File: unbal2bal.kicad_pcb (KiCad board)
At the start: 2 copper layers, 76 x 90 mm, 36 parts, among them J1 RCJ-041, J2 NRJ3HF-1, J3 Mini-DIN-3, J4 Mini-DIN-4, U1 LM4562

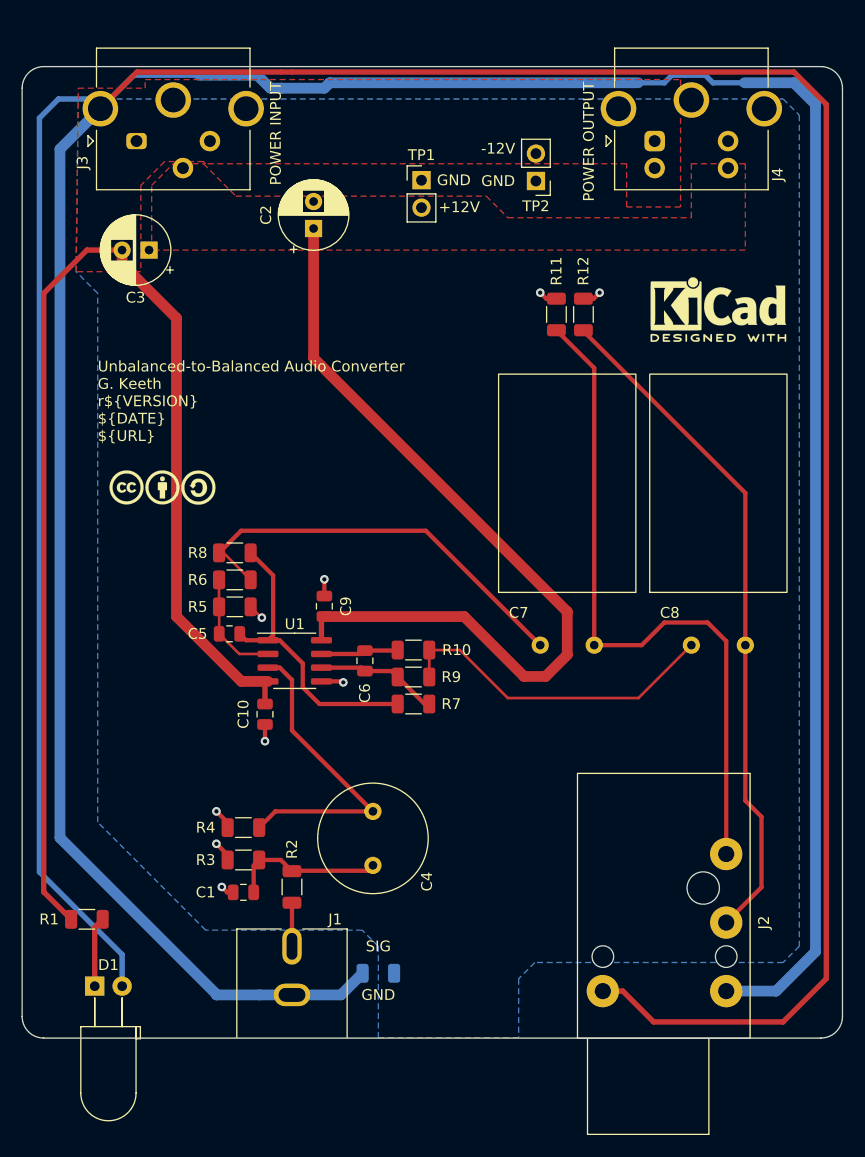
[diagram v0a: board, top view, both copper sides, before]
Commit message: switch to power DIN connectors on main board
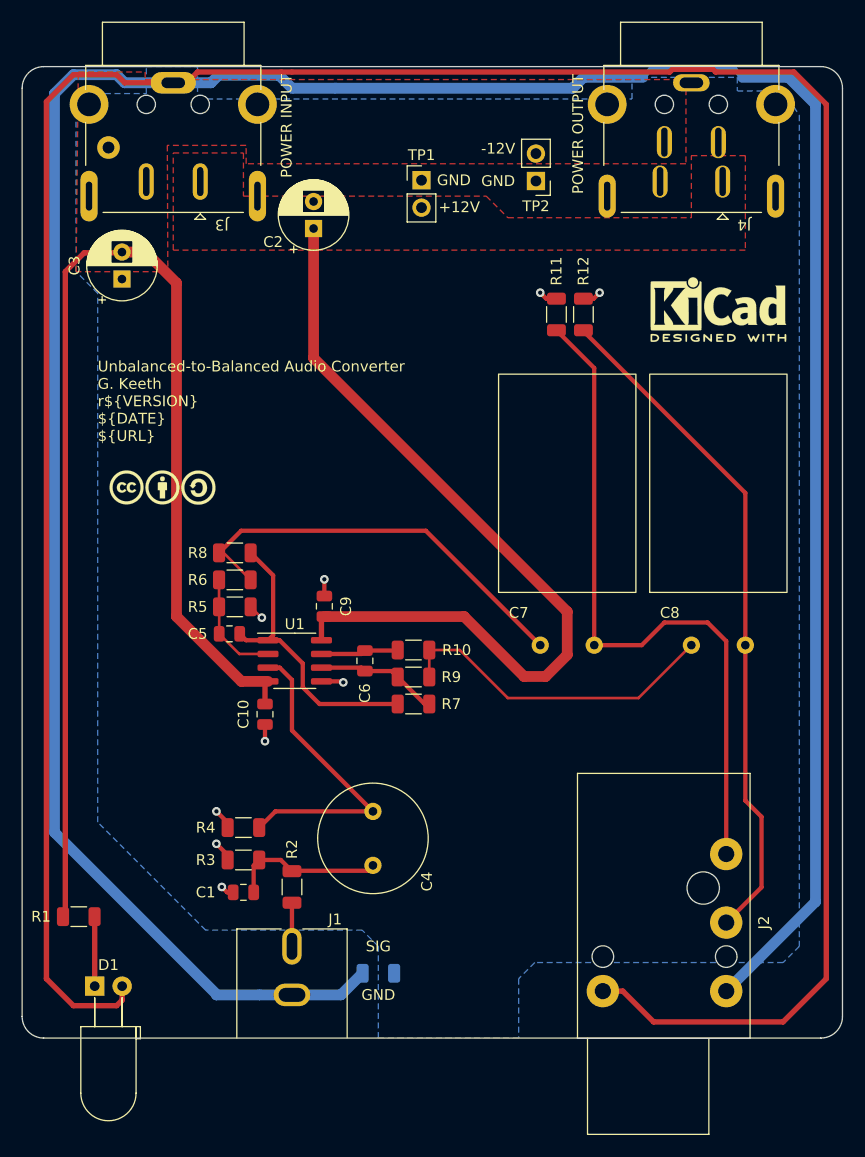
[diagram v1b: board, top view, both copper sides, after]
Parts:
- J3: value Mini-DIN-3 -> CUI_PD-30S; footprint Connector_Mini_DIN_gkeeth:Mini-DIN_Kycon_KMDGX-3S-BS_Horizontal -> Connector_Mini_DIN_gkeeth:Power-DIN_CUI_PD-30S_Horizontal
- J4: value Mini-DIN-4 -> CUI_PD-40S; footprint Connector_Mini_DIN_gkeeth:Mini-DIN_Kycon_KMDGX-4S-BS_Horizontal -> Connector_Mini_DIN_gkeeth:Power-DIN_CUI_PD-40S_Horizontal
- moved J4 7.33 mm to (164.9, 70.7), turned to 180 degrees
- moved J3 6.99 mm to (116.5, 70.7), turned to 180 degrees
- moved C3 3.67 mm to (109.2, 79.7), turned to 90 degrees
- moved NT2 1.00 mm to (127.0, 62.0)
- moved R1 0.79 mm to (105.2, 138.8)
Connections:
- J3 pad 1: VEE -> VCC
- J3 pad 2: GND -> VEE
- J3 pad 3: VCC -> GND
- J4 pad 1: GND -> VCC
- J4 pad 3: VEE -> GND
- J4 pad 4: VCC -> VEE
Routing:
- net GND: track 231.9 -> 243.0 mm
- net Net-(J2-PadS): track 135.4 -> 132.1 mm
- net VEE: track 117.2 -> 116.2 mm
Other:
- board text added: "TODO: Should back panel cutouts be changed to circles for power DIN connectors?"

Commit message: complete TODOs (and fix rev#)
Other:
- board text removed: "TODO: Should back panel cutouts be changed to circles for power DIN connectors?"
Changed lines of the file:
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@@
   (property "DATE" "2022-10-08")
   (property "URL" "github.com/gkeeth/unbal2bal")
-  (property "VERSION" "3")
+  (property "VERSION" "2")
   (net 0 "")
   (net 1 "Net-(C1-Pad1)")
@@
     (effects (font (size 1 1) (thickness 0.15)) (justify left))
   )
-  (gr_text "TODO:\n\nShould back panel cutouts be changed to circles for power DIN connectors?" (at 114.5 23.75) (layer "Cmts.User")
-    (effects (font (size 1 1) (thickness 0.15)) (justify left))
-  )
